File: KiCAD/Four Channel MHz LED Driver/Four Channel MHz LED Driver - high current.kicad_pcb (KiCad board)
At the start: 2 copper layers, 100 x 100 mm, 88 parts, among them J10 Conn_01x24_Female, J2 Conn_01x02_Female, J3 8P8C_Shielded_x4, J4 Conn_01x03_Male, J5 Conn_01x03_Female, J6 Conn_01x08_Female, J7 Conn_01x03_Female, J8 Conn_01x05_Female, J9 Conn_01x24_Female, M1 Fan_4pin, Q1 SUM70060E, SW1 Pushbutton_with_LED, SW2 Pushbutton_with_LED, SW3 Pushbutton_with_LED, SW4 Pushbutton_with_LED, SW5 SW_SPDT, U1 12V boost, U12 Teensy3.6, U2 SN74LV4T125PWR, U3 DPBW06F-05, U4 TMUX1204DGSR, U5 HTSOP-J8_ROM, U6 ADP7182AUJZ-1.8-R7, U7 LT6200CS8-10

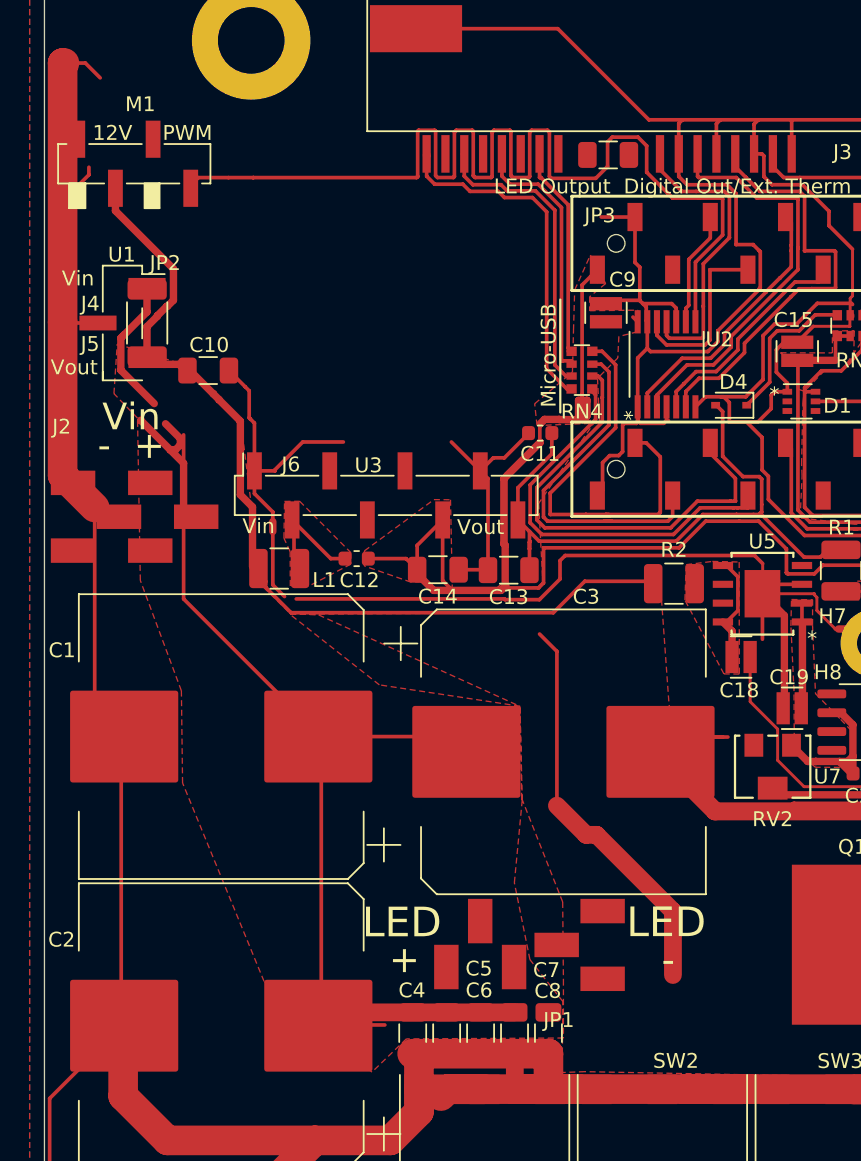
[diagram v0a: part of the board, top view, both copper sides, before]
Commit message: Initial high current design
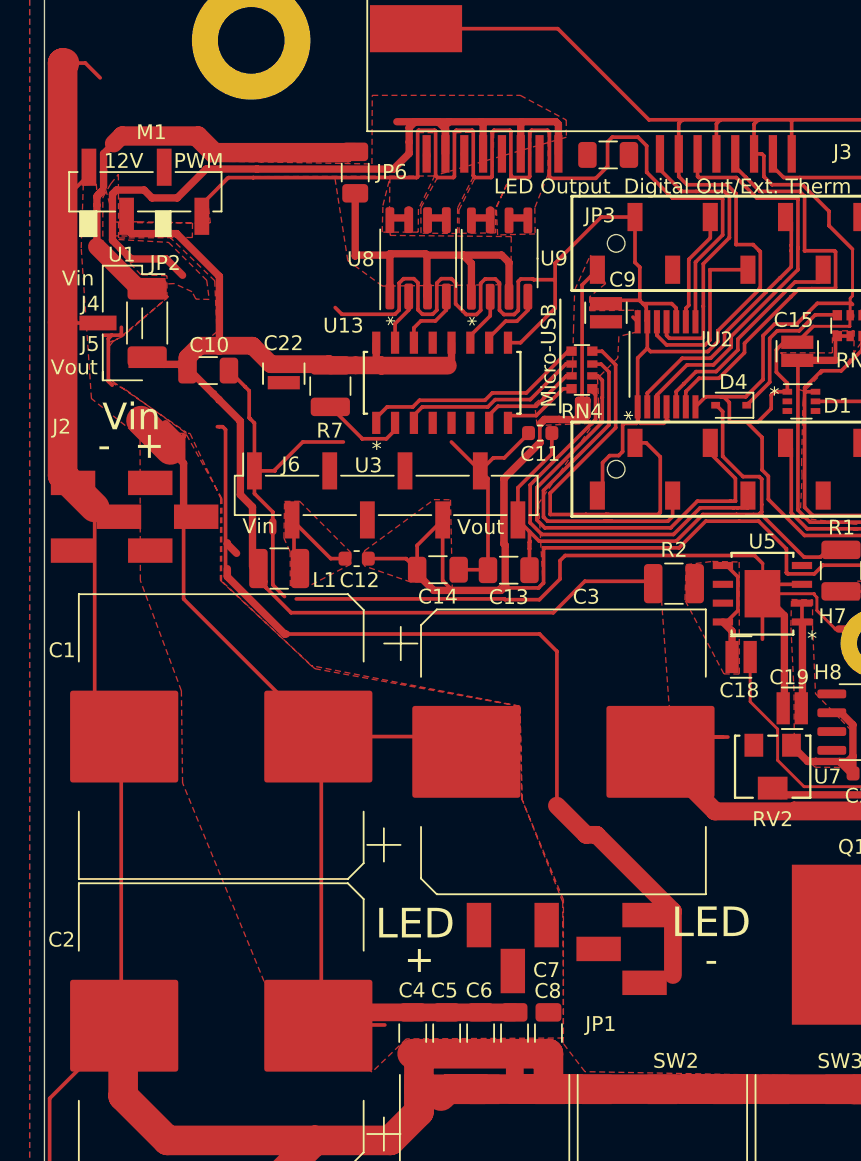
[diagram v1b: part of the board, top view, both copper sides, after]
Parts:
- added C22: 2.2uF, Custom Footprints:0508_Capacitor, F.Cu at (53.1, 54.0)
- added JP6: Jumper_NC_Small, Resistor_SMD:R_1206_3216Metric, F.Cu at (58.0, 40.4)
- added R7: 12, Resistor_SMD:R_1210_3225Metric, F.Cu at (56.3, 54.8)
- added U13: EL7457CSZ-T7, Custom Footprints:EL7457CS, F.Cu at (63.8, 54.6)
- added U8: IRF9358TRPBF, Package_SO:SO-8_3.9x4.9mm_P1.27mm, F.Cu at (62.2, 46.2)
- added U9: IRF9358TRPBF, Package_SO:SO-8_3.9x4.9mm_P1.27mm, F.Cu at (67.7, 46.2)
- moved JP1 2.84 mm to (70.1, 89.7)
- moved M1 2.03 mm to (43.8, 41.7)
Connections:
- J3 pad 2: GND -> /LED-
- J3 pad 4: GND -> /LED-
- J3 pad 6: GND -> /LED-
- J3 pad 8: GND -> /LED-
- RN4 pad 5: Net-(J3-Pad7) -> Net-(RN4-Pad5)
- RN4 pad 6: Net-(J3-Pad5) -> Net-(RN4-Pad6)
- RN4 pad 7: Net-(J3-Pad3) -> Net-(RN4-Pad7)
- RN4 pad 8: Net-(J3-Pad1) -> Net-(RN4-Pad8)
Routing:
- net /LED-: track 27.2 -> 119.2 mm
- net /Vin: track 90.9 -> 139.0 mm
- net GND: track 1122.6 -> 1163.5 mm
- net /Vcc: track 0.00 -> 25.9 mm
- net /12V: track 69.8 -> 94.7 mm
- net Net-(J3-Pad1): track 24.5 -> 2.89 mm
- net Net-(J3-Pad3): track 20.5 -> 1.66 mm
- net Net-(RN4-Pad5): track 0.00 -> 15.4 mm
- net Net-(J3-Pad5): track 17.6 -> 2.43 mm
- net Net-(J3-Pad7): track 14.5 -> 1.27 mm
- net Net-(RN4-Pad6): track 0.00 -> 12.6 mm
- net Net-(RN4-Pad7): track 0.00 -> 7.18 mm
- net Net-(R7-Pad2): track 0.00 -> 6.00 mm
- net Net-(RN4-Pad8): track 0.00 -> 5.44 mm
- net Net-(U13-Pad14): track 0.00 -> 5.16 mm
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- added copper zone on F.Cu, net /12V
- added copper zone on F.Cu, net /Vcc
- added copper zone on F.Cu, net Net-(J3-Pad1)
- added copper zone on F.Cu, net Net-(J3-Pad3)
- added copper zone on F.Cu, net Net-(J3-Pad5)
- added copper zone on F.Cu, net Net-(J3-Pad7)
